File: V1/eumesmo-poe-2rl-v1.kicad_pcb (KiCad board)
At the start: 4 copper layers, 82.5 x 45 mm, 105 parts, among them J1 USB_C_Receptacle_USB2.0, J2 250-202, J3 RJ45 JACK, J4 250-202, K1 G5NB-1A-E-DC5, K2 G5NB-1A-E-DC5, Q1 UMH3N, Q2 MMBT2222A, Q3 WPM2015-3/TR, Q4 LMUN2211LT1G, Q5 MMBT2222A, SW1 RESET, U1 CH340K, U2 ESP32-WROOM-32UE-N16, U3 LAN8710A, U4 TPS2376DDAR-H, U5 TX4138, U6 SY8089A1AAC

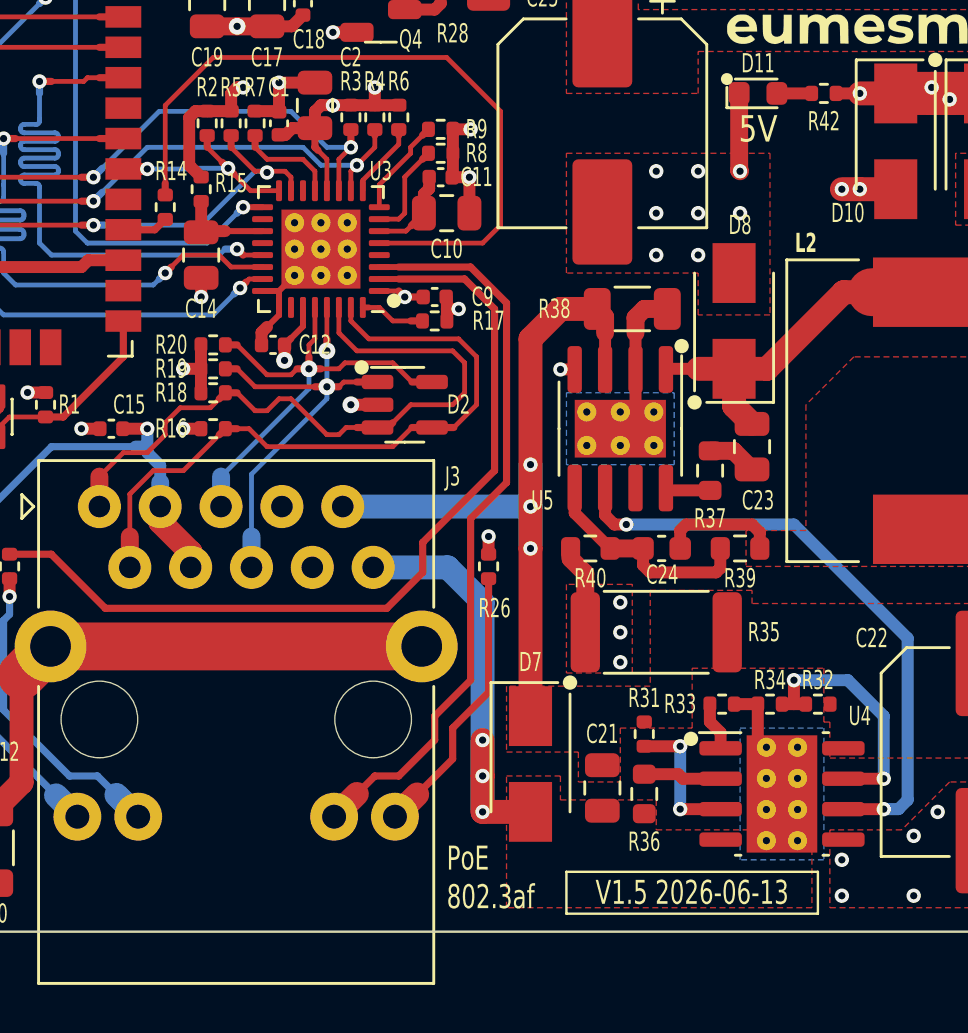
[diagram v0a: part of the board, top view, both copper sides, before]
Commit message: Widened tracks at pads and vias
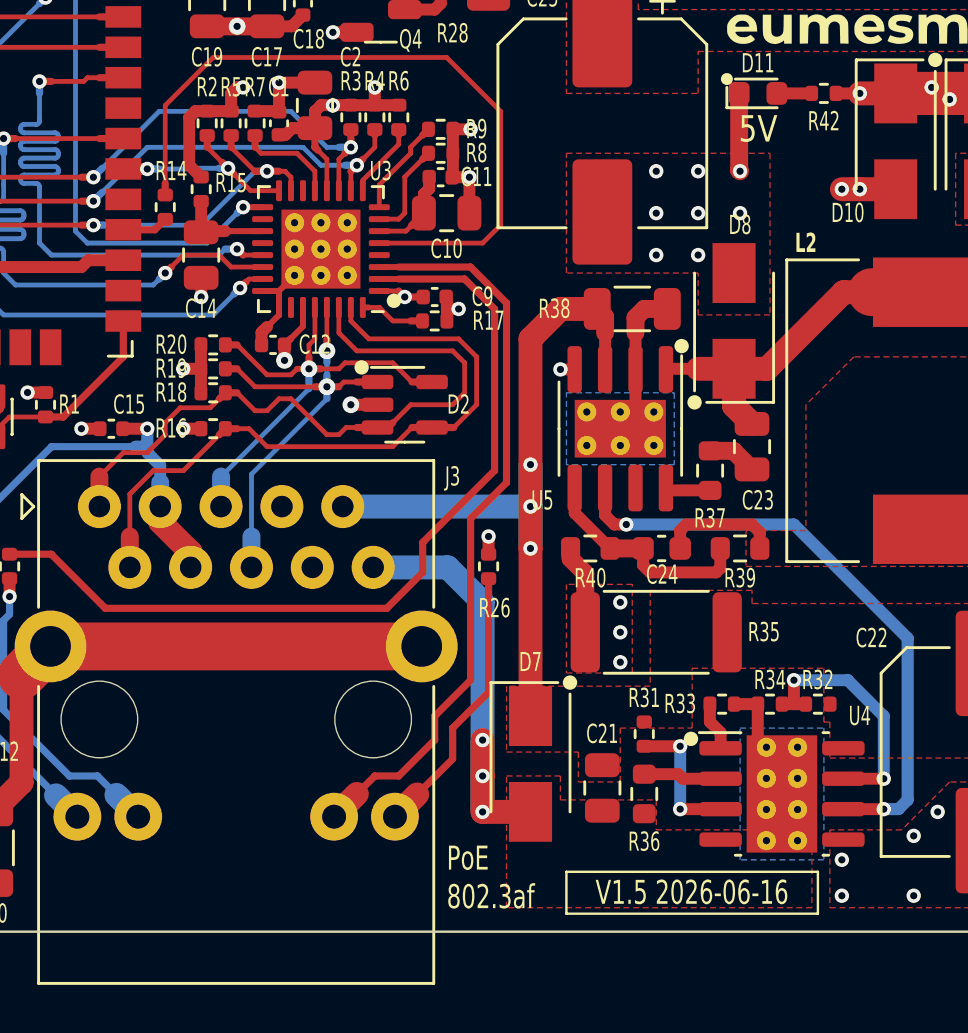
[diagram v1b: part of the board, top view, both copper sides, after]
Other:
- board text added: "V1.5 2026-06-16"
- board text removed: "V1.5 2026-06-13"
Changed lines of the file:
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@@
 		)
 	)
-	(gr_text "V1.5 2026-06-13"
+	(gr_text "V1.5 2026-06-16"
 		(at 141 114.375 0)
 		(layer "F.SilkS")
@@
 			(units 3)
 			(units_format 1)
-			(precision 4)
+			(precision 1)
 		)
 		(style
@@
 			(keep_text_aligned yes)
 		)
-		(gr_text "45.0000 mm"
+		(gr_text "45.0 mm"
 			(at 71.35 93.5 90)
 			(layer "Dwgs.User")
@@
 			(units 3)
 			(units_format 1)
-			(precision 4)
+			(precision 1)
 		)
 		(style
@@
 			(keep_text_aligned yes)
 		)
-		(gr_text "82.5000 mm"
+		(gr_text "82.5 mm"
 			(at 117.25 66.35 0)
 			(layer "Dwgs.User")
@@
 		(start 124.5 92.5)
 		(end 125 92.5)
-		(width 0.3)
+		(width 0.25)
 		(layer "F.Cu")
 		(net "/ETHTXD-")
@@
 		(start 125 92.5)
 		(end 125 93.33)
-		(width 0.2)
+		(width 0.3)
 		(layer "B.Cu")
 		(net "/ETHTXD-")
@@
 	)
 	(segment
+		(start 127.75 83.25)
+		(end 127.25 83.75)
+		(width 0.2)
+		(layer "F.Cu")
+		(net "/EMACRXD1")
+	)
+	(segment
 		(start 126.75 84.25)
 		(end 126.75 85.0625)
@@
 	)
 	(segment
-		(start 127.75 83.25)
+		(start 127.25 83.75)
 		(end 127 84)
-		(width 0.2)
+		(width 0.3)
 		(layer "F.Cu")
 		(net "/EMACRXD1")
@@
 		(start 127 84)
 		(end 126.75 84.25)
-		(width 0.2)
+		(width 0.3)
 		(layer "F.Cu")
 		(net "/EMACRXD1")
@@
 	)
 	(segment
-		(start 125.5 84)
+		(start 126.5 84)
 		(end 127 84)
-		(width 0.2)
+		(width 0.3)
 		(layer "B.Cu")
 		(net "/EMACRXD1")
@@
 	)
 	(segment
+		(start 125.5 84)
+		(end 126.5 84)
+		(width 0.2)
+		(layer "B.Cu")
+		(net "/EMACRXD1")
+	)
+	(segment
 		(start 124.75 83.25)
 		(end 125.5 84)
@@
 	)
 	(segment
-		(start 126.75 83.25)
+		(start 126.5 83.5)
 		(end 126.25 83.75)
 		(width 0.2)
@@
 	)
 	(segment
+		(start 126.75 83.25)
+		(end 126.5 83.5)
+		(width 0.3)
+		(layer "F.Cu")
+		(net "/EMACRXD0")
+	)
+	(segment
 		(start 126.25 83.75)
 		(end 126.25 85.0625)
@@
 	)
 	(segment
+		(start 125.75 83.25)
+		(end 126.25 83.25)
+		(width 0.2)
+		(layer "B.Cu")
+		(net "/EMACRXD0")
+	)
+	(segment
 		(start 124.25 81.75)
 		(end 125.75 83.25)
@@
 	)
 	(segment
-		(start 125.75 83.25)
+		(start 126.25 83.25)
 		(end 126.75 83.25)
-		(width 0.2)
+		(width 0.3)
 		(layer "B.Cu")
 		(net "/EMACRXD0")
 	)
 	(segment
-		(start 125.25 84.25)
-		(end 125.25 85.0625)
-		(width 0.2)
+		(start 122.75 82.76)
+		(end 122.75 83.25)
+		(width 0.3)
 		(layer "F.Cu")
 		(net "/EMACRXD4")
 	)
 	(segment
-		(start 124.75 83.75)
-		(end 125.25 84.25)
+		(start 123 83.5)
+		(end 124.5 83.5)
 		(width 0.2)
 		(layer "F.Cu")
@@
 	)
 	(segment
-		(start 122.75 83.25)
-		(end 123.25 83.75)
+		(start 125.25 84.25)
+		(end 125.25 85.0625)
 		(width 0.2)
 		(layer "F.Cu")
@@
 	)
 	(segment
-		(start 122.75 82.76)
-		(end 122.75 83.25)
-		(width 0.3)
+		(start 122.75 83.25)
+		(end 123 83.5)
+		(width 0.2)
 		(layer "F.Cu")
 		(net "/EMACRXD4")
 	)
 	(segment
-		(start 123.25 83.75)
-		(end 124.75 83.75)
+		(start 124.5 83.5)
+		(end 125.25 84.25)
 		(width 0.2)
 		(layer "F.Cu")
@@
 	)
 	(segment
-		(start 106.066605 86.764)
-		(end 106.066605 86.836)
+		(start 124.25 84.5)
+		(end 124.25 85.0625)
 		(width 0.2)
 		(layer "F.Cu")
@@
 	)
 	(segment
-		(start 124 84.25)
-		(end 124.25 84.5)
+		(start 123.75 84.25)
+		(end 124 84.25)
 		(width 0.2)
 		(layer "F.Cu")
@@
 	)
 	(segment
-		(start 123.25 84.302)
-		(end 123.198 84.25)
-		(width 0.2)
+		(start 123.25 84.25)
+		(end 122.745 84.25)
+		(width 0.3)
 		(layer "F.Cu")
 		(net "/EMACRX")
 	)
 	(segment
-		(start 123.302 84.25)
-		(end 124 84.25)
+		(start 106.066605 86.764)
+		(end 106.066605 86.836)
 		(width 0.2)
 		(layer "F.Cu")
@@
 	)
 	(segment
+		(start 122.745 84.25)
+		(end 121.75 83.255)
+		(width 0.2)
+		(layer "F.Cu")
+		(net "/EMACRX")
+	)
+	(segment
 		(start 108.310605 86.5)
 		(end 115.5 86.5)
@@
 	)
 	(segment
-		(start 123.198 84.25)
-		(end 122.745 84.25)
-		(width 0.2)
+		(start 123.25 84.25)
+		(end 123.75 84.25)
+		(width 0.3)
 		(layer "F.Cu")
 		(net "/EMACRX")
@@
 	)
 	(segment
-		(start 123.25 84.302)
-		(end 123.302 84.25)
-		(width 0.2)
-		(layer "F.Cu")
-		(net "/EMACRX")
-	)
-	(segment
 		(start 115.5 86.5)
 		(end 116 86.5)
@@
 	)
 	(segment
-		(start 108.046605 86.836)
-		(end 108.046605 86.764)
-		(width 0.2)
-		(layer "F.Cu")
-		(net "/EMACRX")
-	)
-	(segment
-		(start 124.25 84.5)
-		(end 124.25 85.0625)
+		(start 124 84.25)
+		(end 124.25 84.5)
 		(width 0.2)
 		(layer "F.Cu")
@@
 	)
 	(segment
-		(start 122.745 84.25)
-		(end 121.75 83.255)
+		(start 108.046605 86.836)
+		(end 108.046605 86.764)
 		(width 0.2)
 		(layer "F.Cu")
@@
 	)
 	(via
-		(at 123.25 84.302)
+		(at 123.25 84.25)
 		(size 0.6)
 		(drill 0.3)
@@
 	)
 	(segment
-		(start 116.5 86.5)
-		(end 120.5 86.5)
-		(width 0.2)
+		(start 122.75 84.25)
+		(end 123.25 84.25)
+		(width 0.3)
 		(layer "B.Cu")
 		(net "/EMACRX")
 	)
 	(segment
-		(start 120.5 86.5)
-		(end 122.75 84.25)
-		(width 0.2)
+		(start 116 86.5)
+		(end 116.5 86.5)
+		(width 0.3)
 		(layer "B.Cu")
 		(net "/EMACRX")
 	)
 	(segment
-		(start 123.198 84.25)
-		(end 123.25 84.302)
+		(start 120.5 86.5)
+		(end 122.75 84.25)
 		(width 0.2)
 		(layer "B.Cu")
@@
 	)
 	(segment
-		(start 122.75 84.25)
-		(end 123.198 84.25)
+		(start 116.5 86.5)
+		(end 120.5 86.5)
 		(width 0.2)
 		(layer "B.Cu")
@@
 	)
 	(segment
-		(start 116 86.5)
-		(end 116.5 86.5)
-		(width 0.3)
-		(layer "B.Cu")
-		(net "/EMACRX")
-	)
-	(segment
 		(start 118.25 84.155)
 		(end 117.25 84.155)
@@
 	(segment
 		(start 121.625 84.125)
+		(end 121.25 84.125)
+		(width 0.3)
+		(layer "B.Cu")
+		(net "/EMACMDIO")
+	)
+	(segment
+		(start 121.25 84.125)
 		(end 120.375 84.125)
 		(width 0.2)
@@
 	)
 	(segment
-		(start 120.345 84.155)
+		(start 118.75 84.155)
 		(end 118.25 84.155)
-		(width 0.2)
+		(width 0.3)
 		(layer "B.Cu")
 		(net "/EMACMDIO")
@@
 	)
 	(segment
+		(start 120.345 84.155)
+		(end 118.75 84.155)
+		(width 0.2)
+		(layer "B.Cu")
+		(net "/EMACMDIO")
+	)
+	(segment
 		(start 115.5 75.5)
 		(end 115.735 75.265)
@@
 	)
 	(segment
+		(start 125.75 93.25)
+		(end 125.75 92.75)
+		(width 0.3)
+		(layer "B.Cu")
+		(net "/ETHTXD+")
+	)
+	(segment
+		(start 125.75 92.75)
+		(end 125.75 92.25)
+		(width 0.2)
+		(layer "B.Cu")
+		(net "/ETHTXD+")
+	)
+	(segment
 		(start 122.6 96.9)
 		(end 125.75 93.75)
@@
 	)
 	(segment
-		(start 125.75 93.25)
+		(start 125.75 92.25)
 		(end 125.75 91.75)
-		(width 0.2)
+		(width 0.3)
 		(layer "B.Cu")
 		(net "/ETHTXD+")
@@
 		(start 125.75 93.75)
 		(end 125.75 93.25)
-		(width 0.2)
+		(width 0.3)
 		(layer "B.Cu")
 		(net "/ETHTXD+")
@@
 		(end 127.8625 94.95)
 		(width 0.3)
-		(layer "F.Cu")
-		(net "/ETHRXD-")
-	)
-	(segment
-		(start 128.3 94.95)
-		(end 127.8625 94.95)
-		(width 0.3)

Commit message: Release V1.5.0
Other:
- board text added: "V1.5 2026-06-17"
- board text removed: "V1.5 2026-06-16"
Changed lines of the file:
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@@
 	(title_block
 		(title "eumesmo 2x Relay Output Module with PoE")
-		(date "2026-06-13")
+		(date "2026-06-17")
 		(rev "V1.5")
 	)
@@
 			(unit
 				(name "A")
-				(pins "3" "4" "5" "21" "22" "17" "18" "20" "19" "32" "2" "1" "38" "15"
-					"39" "25" "35" "24" "34" "26" "29" "14" "16" "13" "23" "27" "28" "30"
+				(pins "3" "4" "5" "21" "22" "17" "18" "20" "19" "32" "2" "1" "38" "39"
+					"15" "25" "35" "24" "34" "26" "29" "14" "16" "13" "23" "27" "28" "30"
 					"31" "33" "36" "37" "10" "11" "12" "8" "9" "6" "7"
 				)
@@
 		)
 	)
-	(gr_text "V1.5 2026-06-16"
+	(gr_text "V1.5 2026-06-17"
 		(at 141 114.375 0)
 		(layer "F.SilkS")

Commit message: Added CPU health LED
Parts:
- removed the D11 at (143.8, 81.0)
- removed the R42 at (146.5, 81.0)
- added D3: WHITE/0603, Tales:LED_0603_1608Metric, F.Cu at (110.2, 99.5)
- added D8: WHITE, Tales:LED_0603_1608Metric, F.Cu at (121.0, 77.0)
- added R15: 300R, Tales:R_0402_1005Metric, F.Cu at (114.2, 94.5)
- added R37: 300R, Tales:R_0402_1005Metric, F.Cu at (120.5, 73.5)
- added REF**: Icon_Heart_Flash, Tales:Icon_Heart_Flash, F.Cu at (108.2, 99.5)
- added REF**: Icon_Power_Plug, Tales:Icon_Power_Plug, F.Cu at (119.5, 77.0)
- moved G*** 11.7 mm to (145.0, 82.2)
- moved R1 3.69 mm to (112.2, 97.2), turned to 0 degrees
- moved C16 3.48 mm to (135.8, 74.2), turned to 180 degrees
- moved C17 2.50 mm to (125.8, 77.2)
- moved C18 2.50 mm to (127.2, 77.2)
- moved C19 2.50 mm to (123.2, 77.2)
- moved L1 2.50 mm to (124.5, 74.5)
- moved Q2 2.25 mm to (130.2, 74.5)
- moved Q3 2.25 mm to (130.2, 77.5)
- moved R22 2.25 mm to (132.8, 74.0)
- moved R24 2.25 mm to (132.8, 76.0)
- renumbered D4 to D10, D5 to D11, D6 to D12, D7 to D4, D8 to D5, D9 to D6, D10 to D7, D3 to D9, J3 to J2, J2 to J3, Q3 to Q2, Q4 to Q3, Q2 to Q4, R15 to R16, R16 to R17, R17 to R18, R18 to R19, R19 to R20, R20 to R21, R25 to R22, R24 to R23, R28 to R24, R26 to R25, R31 to R26, R32 to R27, R33 to R28, R34 to R29, R35 to R30, R36 to R31, R37 to R32, R38 to R33, R39 to R34, R40 to R35, R41 to R36, R43 to R38, R21 to R39, R22 to R40, R23 to R41, R27 to R42, R29 to R43, R30 to R44
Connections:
- J3 pad 1: /RELAY OUTPUTS/OUT1LN -> /RELAY OUTPUTS/OUT1LD
- J3 pad 2: /RELAY OUTPUTS/OUT1LD -> /RELAY OUTPUTS/OUT1LN
- J4 pad 1: /RELAY OUTPUTS/OUT2LN -> /RELAY OUTPUTS/OUT2LD
- J4 pad 2: /RELAY OUTPUTS/OUT2LD -> /RELAY OUTPUTS/OUT2LN
- U2 pad 24: unconnected-(U2-IO2-Pad24) -> /CPUOK
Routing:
- net /RELAY OUTPUTS/OUT1LN: track 15.9 -> 41.0 mm
- net /RELAY OUTPUTS/OUT2LN: track 16.5 -> 41.4 mm
- net /CPULED: track 0.00 -> 7.14 mm
- net /CPUOK: track 0.00 -> 4.27 mm, vias 0 -> 2
- net PHYPWR: track 44.7 -> 47.9 mm
- net /POWER/3V3LED: track 0.00 -> 2.72 mm
- net +5V: track 104.1 -> 101.6 mm, vias 7 -> 6
- net GND: track 70.3 -> 72.7 mm
- net /ESPPROG: track 8.38 -> 10.5 mm
- net /UARTNDTR: track 11.7 -> 13.1 mm
- net /POWER/PWRON: track 1.45 -> 0.00 mm
- net /RELAY OUTPUTS/OUT2LD: track 16.0 -> 14.5 mm
- net /PHYPWRFET: track 5.48 -> 4.07 mm
- net +3V3: track 40.1 -> 38.8 mm, vias 10 -> 11
- net +3V3LAN: track 19.9 -> 21.2 mm
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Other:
- board text added: "RST"
- board text removed: "5V"
- board text removed: "RESET"
